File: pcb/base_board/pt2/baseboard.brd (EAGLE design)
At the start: 88 x 85 mm, 40 parts, among them IC1 LD117AS33TR, P1 RPI3NO-CONNECTORS, SW1 324_SW, SW2 324_SW, SW20 324_SW, SW3 324_SW, SW4 324_SW, U5 CH340C

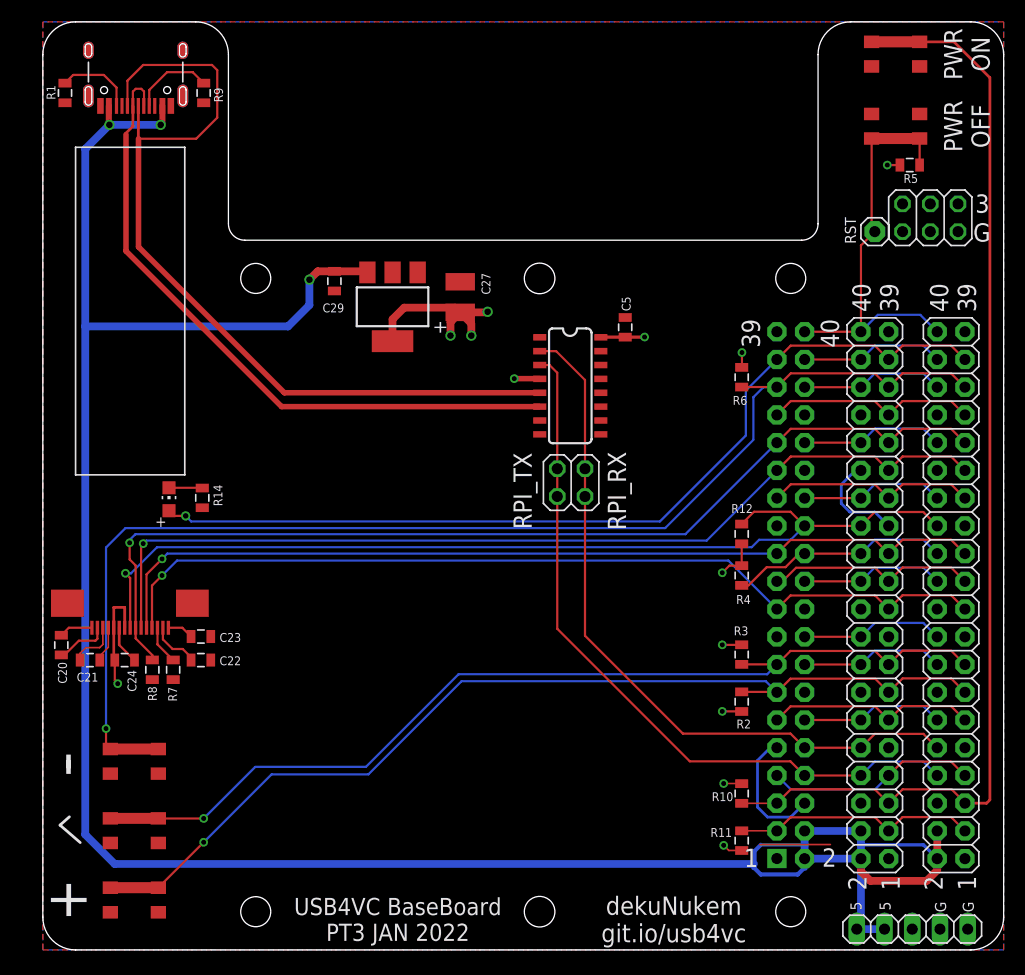
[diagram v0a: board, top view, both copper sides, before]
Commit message: added sleep LED on baseboard
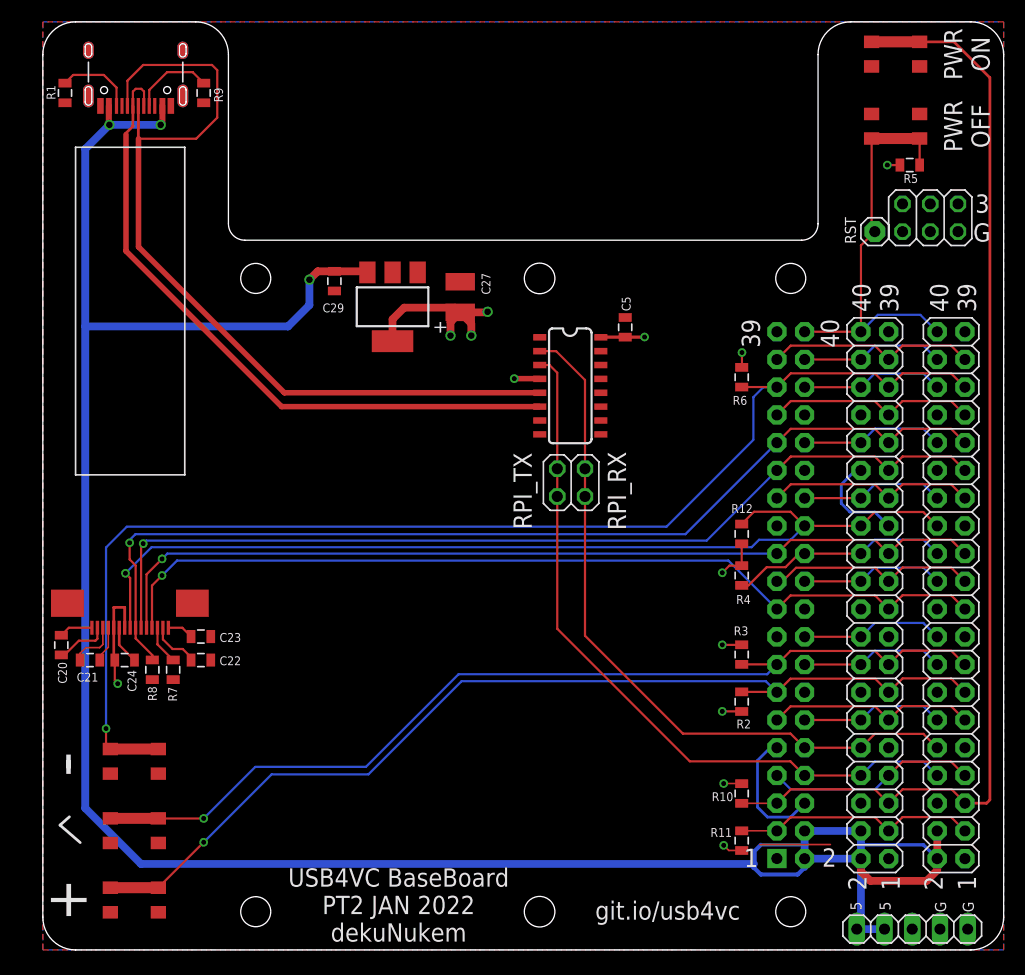
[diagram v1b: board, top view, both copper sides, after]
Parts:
- removed LED1: (no value), adafruit:CHIP-LED0805
- removed R14: 2K, SparkFun-Passives:0805
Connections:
- removed net N$10: LED1.C, R14.2
- removed net N$4: LED1.A, P1.P$37, P2.37, P3.37
- new net N$21: P1.P$37, P2.37, P3.37
- net GND: no longer R14.1
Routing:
- net N$4: track 84.0 -> 0.00 mm, vias 1 -> 0
- net N$21: track 0.00 -> 19.3 mm
- net N$10: track 3.06 -> 0.00 mm
- net +5V: track 222.8 -> 221.4 mm
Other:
- board text added: "USB4VC BaseBoard PT2 JAN 2022 dekuNukem"
- board text added: "git.io/usb4vc"
- board text removed: "USB4VC BaseBoard PT3 JAN 2022"
- board text removed: "dekuNukem git.io/usb4vc"
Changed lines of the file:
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@@
 <circle x="19.5" y="3.5" radius="3" width="0" layer="42"/>
 <circle x="19.5" y="61.5" radius="3" width="0" layer="42"/>
-<text x="32.512" y="2.794" size="1.5748" layer="25" rot="R180" align="center">USB4VC BaseBoard
-PT3 JAN 2022</text>
+<text x="32.5882" y="4.1148" size="1.6764" layer="25" rot="R180" align="center">USB4VC BaseBoard
+PT2 JAN 2022
+dekuNukem</text>
 <text x="86.0552" y="68.3514" size="1.6764" layer="25" rot="R180" align="center">3</text>
 <text x="86.0044" y="65.7098" size="1.6764" layer="25" rot="R180" align="center">G</text>
@@
 <wire x1="2.4384" y1="12.192" x2="1.5748" y2="11.43" width="0.254" layer="25"/>
 <wire x1="1.5748" y1="11.43" x2="3.429" y2="9.8298" width="0.254" layer="25"/>
-<text x="57.785" y="2.794" size="1.6764" layer="25" rot="R180" align="center">dekuNukem
-git.io/usb4vc</text>
+<text x="57.2262" y="3.6068" size="1.6764" layer="25" rot="R180" align="center">git.io/usb4vc</text>
 <rectangle x1="48.26" y1="0" x2="71.628" y2="8.128" layer="41"/>
 <rectangle x1="48.26" y1="0" x2="71.628" y2="8.128" layer="42"/>
@@
 <attribute name="VALUE" x="74.93" y="62.611" size="1.27" layer="27"/>
 </element>
-<element name="LED1" library="adafruit" package="CHIP-LED0805" value="" x="11.557" y="41.275" smashed="yes">
-<attribute name="VALUE" x="14.097" y="40.005" size="1.27" layer="27" rot="R90"/>
-</element>
-<element name="R14" library="SparkFun-Passives" package="0805" value="2K" x="14.605" y="41.402" smashed="yes" rot="R90">
-<attribute name="NAME" x="16.4465" y="40.64" size="0.8128" layer="25" rot="R90"/>
-</element>
 </elements>
 <signals>
@@
 <contactref element="JP5" pad="5"/>
 <contactref element="JP5" pad="4"/>
-<contactref element="R14" pad="1"/>
 </signal>
 <signal name="+3V3">
@@
 <wire x1="65.7606" y1="9.6266" x2="69.7718" y2="9.6266" width="0.3048" layer="16"/>
 <wire x1="6.096" y1="75.565" x2="3.8862" y2="73.3552" width="0.7112" layer="16"/>
-<wire x1="6.5786" y1="7.874" x2="65.1256" y2="7.874" width="0.7112" layer="16"/>
+<wire x1="8.9916" y1="7.874" x2="65.1256" y2="7.874" width="0.7112" layer="16"/>
 <wire x1="74.93" y1="10.8966" x2="74.93" y2="9.6774" width="0.7112" layer="16"/>
 <wire x1="74.93" y1="8.3566" x2="74.93" y2="9.6774" width="0.7112" layer="16"/>
@@
 <wire x1="69.7718" y1="10.8966" x2="74.93" y2="10.8966" width="0.7112" layer="16"/>
 <wire x1="3.8862" y1="73.3552" x2="3.8862" y2="57.0992" width="0.7112" layer="16"/>
-<wire x1="3.8862" y1="57.0992" x2="3.8862" y2="10.5664" width="0.7112" layer="16"/>
-<wire x1="3.8862" y1="10.5664" x2="6.5786" y2="7.874" width="0.7112" layer="16"/>
+<wire x1="3.8862" y1="57.0992" x2="3.8862" y2="12.9794" width="0.7112" layer="16"/>
+<wire x1="3.8862" y1="12.9794" x2="8.9916" y2="7.874" width="0.7112" layer="16"/>
 <wire x1="3.8862" y1="57.0992" x2="22.4536" y2="57.0992" width="0.7112" layer="16"/>
 <contactref element="JP5" pad="2"/>
@@
 <wire x1="5.7912" y1="20.2692" x2="5.7912" y2="18.7878" width="0.2032" layer="1"/>
 <wire x1="5.7912" y1="18.7878" x2="6.182" y2="18.397" width="0.2032" layer="1"/>
-<wire x1="65.0748" y1="46.7106" x2="56.9976" y2="38.6334" width="0.2032" layer="16"/>
-<wire x1="56.9976" y1="38.6334" x2="7.5692" y2="38.6334" width="0.2032" layer="16"/>
-<wire x1="7.5692" y1="38.6334" x2="5.7912" y2="36.8554" width="0.2032" layer="16"/>
+<wire x1="65.0748" y1="46.7106" x2="57.1246" y2="38.7604" width="0.2032" layer="16"/>
+<wire x1="57.1246" y1="38.7604" x2="7.6962" y2="38.7604" width="0.2032" layer="16"/>
+<wire x1="7.6962" y1="38.7604" x2="5.7912" y2="36.8554" width="0.2032" layer="16"/>
 <wire x1="6.182" y1="18.397" x2="10.582" y2="18.397" width="1.016" layer="1"/>
+</signal>
+<signal name="N$21">
+<contactref element="P2" pad="37"/>
+<contactref element="P1" pad="P$37"/>
+<wire x1="67.2318" y1="54.0766" x2="68.5018" y2="55.3466" width="0.2032" layer="1"/>
+<wire x1="76.2" y1="55.3466" x2="77.47" y2="54.0766" width="0.2032" layer="1"/>
+<wire x1="68.5018" y1="55.3466" x2="76.2" y2="55.3466" width="0.2032" layer="1"/>
+<contactref element="P3" pad="37"/>
+<wire x1="77.47" y1="54.0766" x2="78.74" y2="55.3466" width="0.2032" layer="1"/>
+<wire x1="83.185" y1="55.3466" x2="84.455" y2="54.0766" width="0.2032" layer="1"/>
+<wire x1="78.74" y1="55.3466" x2="83.185" y2="55.3466" width="0.2032" layer="1"/>
 </signal>
 <signal name="N$22">
@@
 <wire x1="76.2" y1="40.1066" x2="80.645" y2="40.1066" width="0.2032" layer="1"/>
 <contactref element="U2" pad="8"/>
-<wire x1="10.4648" y1="36.8808" x2="8.0772" y2="34.4932" width="0.2032" layer="16"/>
-<wire x1="8.0772" y1="34.4932" x2="7.5692" y2="34.4932" width="0.2032" layer="16"/>
+<wire x1="9.9568" y1="36.8808" x2="7.5692" y2="34.4932" width="0.2032" layer="16"/>
 <via x="7.5692" y="34.4932" extent="1-16" drill="0.45"/>
 <wire x1="8" y1="34.0624" x2="7.5692" y2="34.4932" width="0.2032" layer="1"/>
@@
 <wire x1="68.5018" y1="37.5666" x2="65.6082" y2="37.5666" width="0.2032" layer="16"/>
 <wire x1="65.6082" y1="37.5666" x2="64.9224" y2="36.8808" width="0.2032" layer="16"/>
-<wire x1="64.9224" y1="36.8808" x2="10.4648" y2="36.8808" width="0.2032" layer="16"/>
+<wire x1="64.9224" y1="36.8808" x2="9.9568" y2="36.8808" width="0.2032" layer="16"/>
 <contactref element="R12" pad="2"/>
 <wire x1="64.008" y1="39" x2="65.14" y2="40.132" width="0.2032" layer="1"/>
@@
 <wire x1="6.182" y1="5.697" x2="10.582" y2="5.697" width="1.016" layer="1"/>
 </signal>
-<signal name="N$10">
-<contactref element="LED1" pad="C"/>
-<contactref element="R14" pad="2"/>
-<wire x1="11.557" y1="42.325" x2="14.582" y2="42.325" width="0.2032" layer="1"/>
-<wire x1="14.582" y1="42.325" x2="14.605" y2="42.302" width="0.2032" layer="1"/>
-</signal>
-<signal name="N$4">
-<contactref element="LED1" pad="A"/>
-<contactref element="P2" pad="37"/>
-<contactref element="P1" pad="P$37"/>
-<contactref element="P3" pad="37"/>
-<wire x1="67.2318" y1="54.0766" x2="68.5018" y2="55.3466" width="0.2032" layer="1"/>
-<wire x1="76.2" y1="55.3466" x2="77.47" y2="54.0766" width="0.2032" layer="1"/>
-<wire x1="68.5018" y1="55.3466" x2="76.2" y2="55.3466" width="0.2032" layer="1"/>
-<wire x1="77.47" y1="54.0766" x2="78.74" y2="55.3466" width="0.2032" layer="1"/>
-<wire x1="83.185" y1="55.3466" x2="84.455" y2="54.0766" width="0.2032" layer="1"/>
-<wire x1="78.74" y1="55.3466" x2="83.185" y2="55.3466" width="0.2032" layer="1"/>
-<wire x1="67.2318" y1="54.0766" x2="64.389" y2="51.2338" width="0.2032" layer="16"/>
-<wire x1="64.389" y1="47.117" x2="56.515" y2="39.243" width="0.2032" layer="16"/>
-<wire x1="56.515" y1="39.243" x2="13.589" y2="39.243" width="0.2032" layer="16"/>
-<wire x1="13.589" y1="39.243" x2="13.081" y2="39.751" width="0.2032" layer="16"/>
-<via x="13.081" y="39.751" extent="1-16" drill="0.5"/>
-<wire x1="13.081" y1="39.751" x2="12.031" y2="39.751" width="0.2032" layer="1"/>
-<wire x1="12.031" y1="39.751" x2="11.557" y2="40.225" width="0.2032" layer="1"/>
-<wire x1="64.389" y1="51.2338" x2="64.389" y2="47.117" width="0.2032" layer="16"/>
-</signal>
 </signals>
